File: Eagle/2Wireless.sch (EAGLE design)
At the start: 17 parts, among them IC1 TCA9517A, IC2 VREGLD1117, IC3 MB85RS256TYPNF-G-BCERE1, U1 PHOTON_WITH_HEADERS

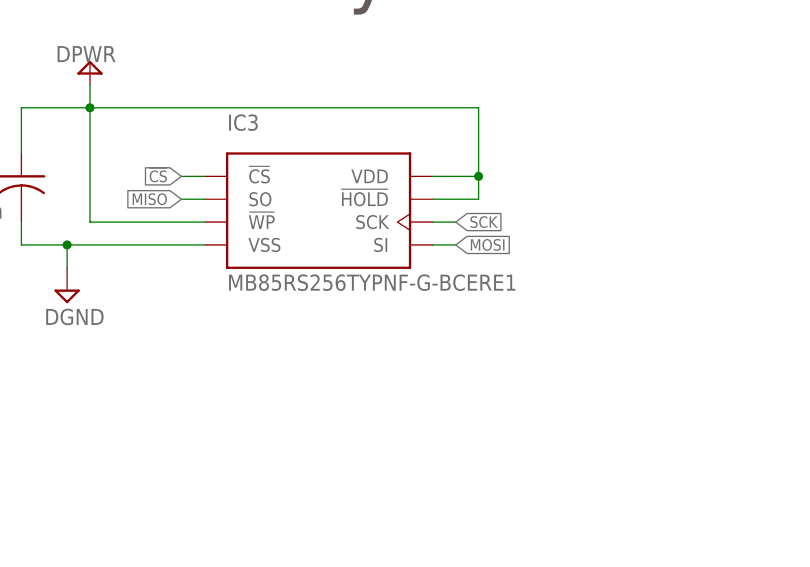
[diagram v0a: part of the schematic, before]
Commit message: Change FRAM to 256k.
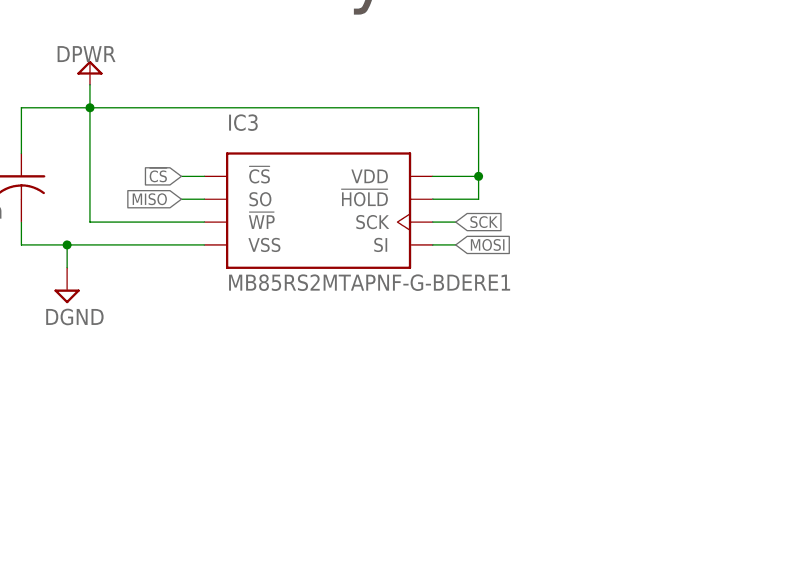
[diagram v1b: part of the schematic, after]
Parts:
- IC3: value MB85RS256TYPNF-G-BCERE1 -> MB85RS2MTAPNF-G-BDERE1
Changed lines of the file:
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@@
 <setting verticaltext="up"/>
 </settings>
-<grid distance="0.1" unitdist="inch" unit="inch" style="lines" multiple="1" display="yes" altdistance="0.01" altunitdist="inch" altunit="inch"/>
+<grid distance="0.1" unitdist="inch" unit="inch" style="lines" multiple="1" display="no" altdistance="0.01" altunitdist="inch" altunit="inch"/>
 <layers>
 <layer number="1" name="Top" color="4" fill="1" visible="no" active="no"/>
@@
 <part name="DGND21" library="studio_h" deviceset="DGND" device=""/>
 <part name="IC2" library="studio_h" deviceset="VREG" device="LD1117"/>
-<part name="IC3" library="studio_h" deviceset="FRAMSPI" device="" value="MB85RS256TYPNF-G-BCERE1"/>
+<part name="IC3" library="studio_h" deviceset="FRAMSPI" device="" value="MB85RS2MTAPNF-G-BDERE1"/>
 <part name="DGND24" library="studio_h" deviceset="DGND" device=""/>
 <part name="C7" library="studio_h" deviceset="C" device="B" value="100n"/>

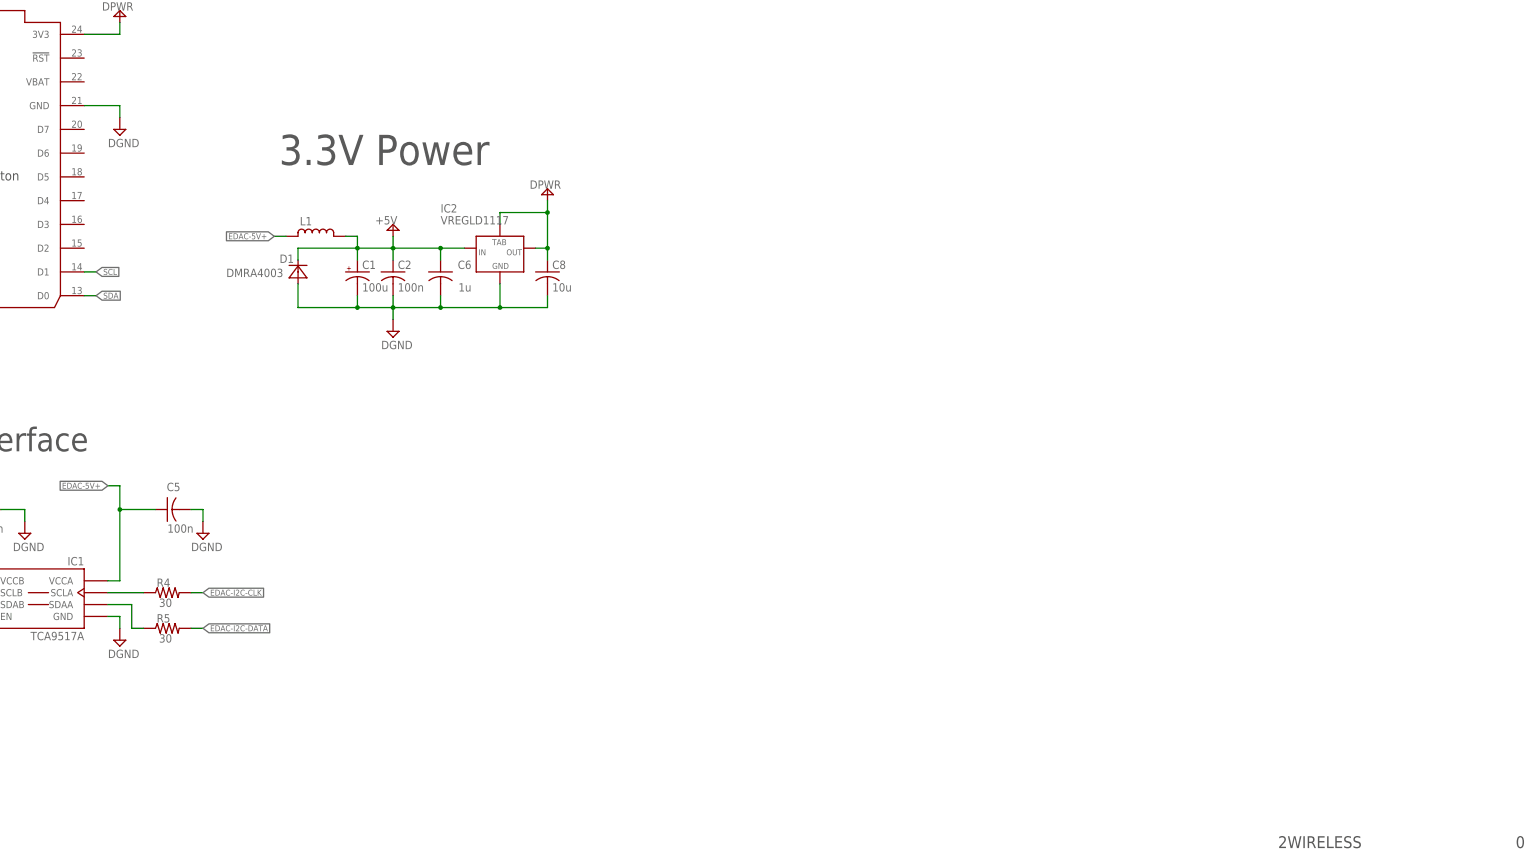
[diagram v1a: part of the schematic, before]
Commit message: Add Primo/V2 version switch.
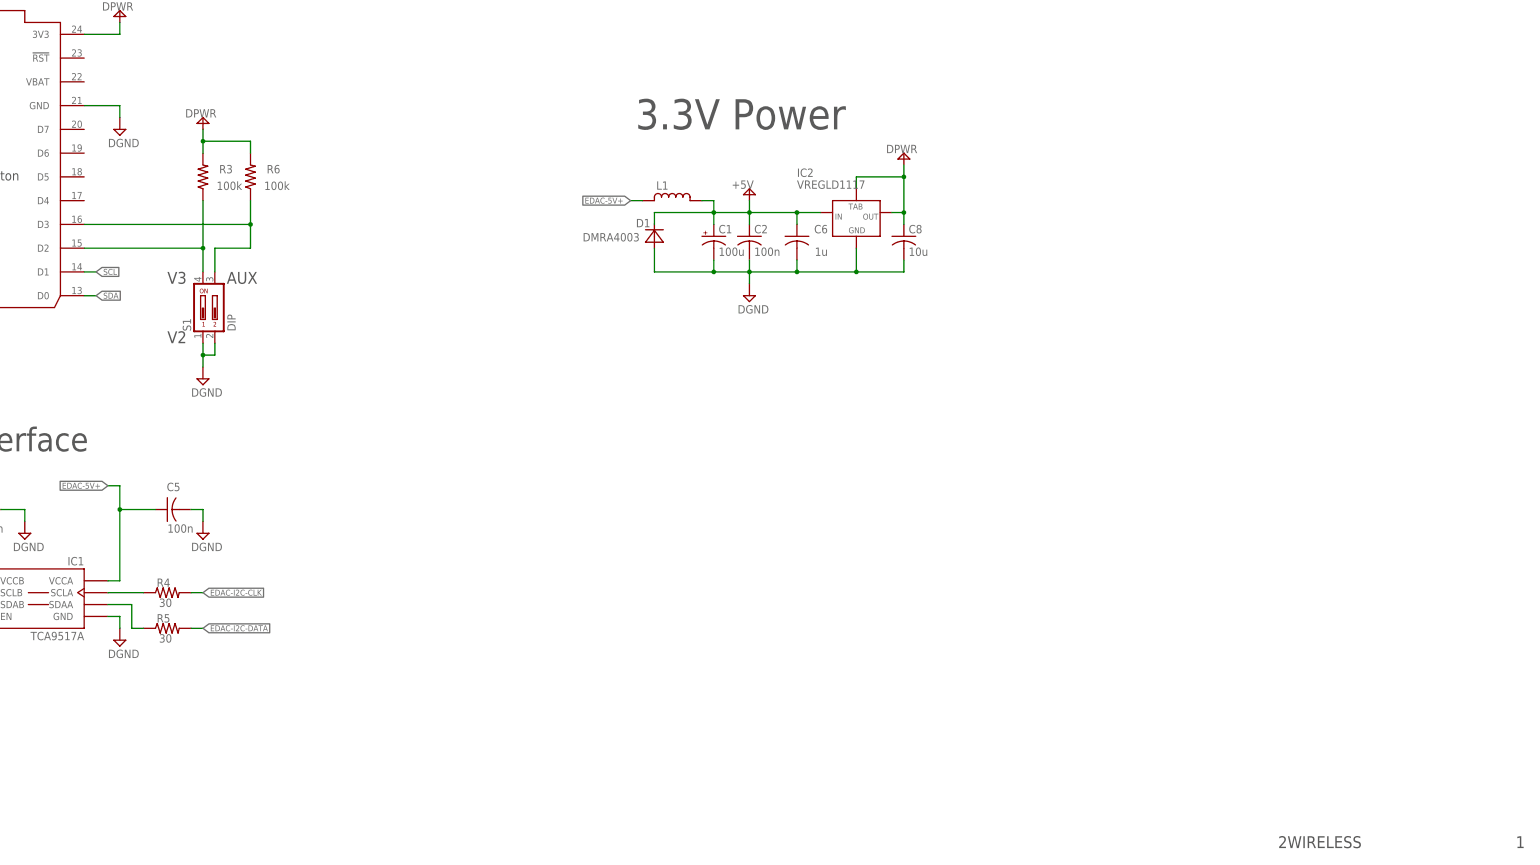
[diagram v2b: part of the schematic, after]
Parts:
- added R3, R6: 100k, studio_h:RB
- added S1: DIP, studio_h:219-02
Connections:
- new net DI-AUX: R6.1, S1.3, U1.D3
- new net DI-VERSION: R3.1, S1.4, U1.D2
- net DGND: now also S1.1, S1.2
- net DPWR: now also R3.2, R6.2
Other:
- note added: "1"
- note added: "AUX"
- note added: "V2"
- note added: "V3"
- note removed: "0"
- moved on the sheet: C1, C2, C6, C8, D1, IC2, L1

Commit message: Add RS232 Connector for future use.
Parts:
- added SV1: (no value), studio_h:MA04-1
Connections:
- new net RX: SV1.4, U1.RX
- new net TX: SV1.3, U1.TX
- net +5V: now also SV1.1
- net DGND: now also SV1.2
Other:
- note added: "2"
- note added: "Male: TE 640456-4 Female: TE 3-640441-4"
- note added: "RS-232"
- note removed: "1"
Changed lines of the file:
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@@
 <part name="DPWR5" library="studio_h" deviceset="DPWR" device=""/>
 <part name="DGND3" library="studio_h" deviceset="DGND" device=""/>
+<part name="SV1" library="studio_h" deviceset="MA04-1" device=""/>
+<part name="DGND4" library="studio_h" deviceset="DGND" device=""/>
 </parts>
 <sheets>
@@
 <plain>
 <text x="367.03" y="6.35" size="2.54" layer="97" font="vector" ratio="12">2WIRELESS</text>
-<text x="417.83" y="6.35" size="2.54" layer="97" font="vector" ratio="12">1</text>
+<text x="417.83" y="6.35" size="2.54" layer="97" font="vector" ratio="12">2</text>
 <text x="229.616" y="160.02" size="6.4516" layer="97" font="vector" ratio="12">3.3V Power</text>
 <text x="237.236" y="233.172" size="6.4516" layer="97" font="vector" ratio="12">Memory</text>
@@
 <text x="129.54" y="114.3" size="2.54" layer="97" font="vector" ratio="12">V2</text>
 <text x="142.24" y="127" size="2.54" layer="97" font="vector" ratio="12">AUX</text>
+<text x="239.776" y="93.98" size="6.4516" layer="97" font="vector" ratio="12">RS-232</text>
+<text x="240.03" y="62.23" size="2.54" layer="97" font="vector" ratio="12">Male: TE 640456-4
+Female: TE 3-640441-4</text>
 </plain>
 <instances>
@@
 </instance>
 <instance part="DGND1" gate="G$1" x="119.38" y="160.02"/>
-<instance part="DGND2" gate="G$1" x="68.58" y="170.18"/>
+<instance part="DGND2" gate="G$1" x="55.88" y="170.18"/>
 <instance part="C4" gate="G$1" x="88.9" y="78.74" smashed="yes" rot="R90">
 <attribute name="NAME" x="91.694" y="84.455" size="1.778" layer="95" font="vector" ratio="12" rot="R180"/>
@@
 <instance part="DPWR5" gate="G$1" x="137.16" y="160.02"/>
 <instance part="DGND3" gate="G$1" x="137.16" y="106.68"/>
+<instance part="SV1" gate="G$1" x="259.08" y="78.74"/>
+<instance part="DGND4" gate="G$1" x="281.94" y="73.66"/>
 </instances>
 <busses>
@@
 <pinref part="U1" gate="G$1" pin="GND@2"/>
 <pinref part="DGND2" gate="G$1" pin="DGND"/>
-<wire x1="76.2" y1="175.26" x2="68.58" y2="175.26" width="0.1524" layer="91"/>
-<wire x1="68.58" y1="175.26" x2="68.58" y2="172.72" width="0.1524" layer="91"/>
+<wire x1="76.2" y1="175.26" x2="55.88" y2="175.26" width="0.1524" layer="91"/>
+<wire x1="55.88" y1="175.26" x2="55.88" y2="172.72" width="0.1524" layer="91"/>
 </segment>
 <segment>
@@
 <wire x1="139.7" y1="111.76" x2="137.16" y2="111.76" width="0.1524" layer="91"/>
 <junction x="137.16" y="111.76"/>
+</segment>
+<segment>
+<pinref part="SV1" gate="G$1" pin="2"/>
+<pinref part="DGND4" gate="G$1" pin="DGND"/>
+<wire x1="264.16" y1="78.74" x2="281.94" y2="78.74" width="0.1524" layer="91"/>
+<wire x1="281.94" y1="78.74" x2="281.94" y2="76.2" width="0.1524" layer="91"/>
 </segment>
 </net>
@@
 <pinref part="IC2" gate="G$1" pin="IN"/>
 </segment>
+<segment>
+<pinref part="SV1" gate="G$1" pin="1"/>
+<wire x1="264.16" y1="76.2" x2="266.7" y2="76.2" width="0.1524" layer="91"/>
+<label x="266.7" y="76.2" size="1.27" layer="95" font="vector" ratio="12" xref="yes"/>
+</segment>
 </net>
 <net name="EDAC-5V+" class="0">
@@
 <segment>
 <pinref part="U1" gate="G$1" pin="A5"/>
-<wire x1="76.2" y1="149.86" x2="71.12" y2="149.86" width="0.1524" layer="91"/>
-<label x="71.12" y="149.86" size="1.27" layer="95" font="vector" ratio="12" rot="R180" xref="yes"/>
+<wire x1="76.2" y1="149.86" x2="73.66" y2="149.86" width="0.1524" layer="91"/>
+<label x="73.66" y="149.86" size="1.27" layer="95" font="vector" ratio="12" rot="R180" xref="yes"/>
 </segment>
 <segment>
@@
 <segment>
 <pinref part="U1" gate="G$1" pin="A4"/>
-<wire x1="76.2" y1="144.78" x2="71.12" y2="144.78" width="0.1524" layer="91"/>
-<label x="71.12" y="144.78" size="1.27" layer="95" font="vector" ratio="12" rot="R180" xref="yes"/>
+<wire x1="76.2" y1="144.78" x2="73.66" y2="144.78" width="0.1524" layer="91"/>
+<label x="73.66" y="144.78" size="1.27" layer="95" font="vector" ratio="12" rot="R180" xref="yes"/>
 </segment>
 <segment>
@@
 <segment>
 <pinref part="U1" gate="G$1" pin="A3"/>
-<wire x1="76.2" y1="139.7" x2="71.12" y2="139.7" width="0.1524" layer="91"/>
-<label x="71.12" y="139.7" size="1.27" layer="95" font="vector" ratio="12" rot="R180" xref="yes"/>
+<wire x1="76.2" y1="139.7" x2="73.66" y2="139.7" width="0.1524" layer="91"/>
+<label x="73.66" y="139.7" size="1.27" layer="95" font="vector" ratio="12" rot="R180" xref="yes"/>
 </segment>
 <segment>
@@
 <segment>
 <pinref part="U1" gate="G$1" pin="A2"/>
-<wire x1="76.2" y1="134.62" x2="71.12" y2="134.62" width="0.1524" layer="91"/>
-<label x="71.12" y="134.62" size="1.27" layer="95" font="vector" ratio="12" rot="R180" xref="yes"/>
+<wire x1="76.2" y1="134.62" x2="73.66" y2="134.62" width="0.1524" layer="91"/>
+<label x="73.66" y="134.62" size="1.27" layer="95" font="vector" ratio="12" rot="R180" xref="yes"/>
 </segment>
 <segment>
@@
 </segment>
 </net>
+<net name="TX" class="0">
+<segment>
+<pinref part="U1" gate="G$1" pin="TX"/>
+<wire x1="76.2" y1="170.18" x2="73.66" y2="170.18" width="0.1524" layer="91"/>
+<label x="73.66" y="170.18" size="1.27" layer="95" font="vector" ratio="12" rot="R180" xref="yes"/>
+</segment>
+<segment>
+<pinref part="SV1" gate="G$1" pin="3"/>
+<wire x1="264.16" y1="81.28" x2="266.7" y2="81.28" width="0.1524" layer="91"/>
+<label x="266.7" y="81.28" size="1.27" layer="95" font="vector" ratio="12" xref="yes"/>
+</segment>
+</net>
+<net name="RX" class="0">
+<segment>
+<pinref part="U1" gate="G$1" pin="RX"/>
+<wire x1="76.2" y1="165.1" x2="73.66" y2="165.1" width="0.1524" layer="91"/>
+<label x="73.66" y="165.1" size="1.27" layer="95" font="vector" ratio="12" rot="R180" xref="yes"/>
+</segment>
+<segment>
+<pinref part="SV1" gate="G$1" pin="4"/>
+<wire x1="264.16" y1="83.82" x2="266.7" y2="83.82" width="0.1524" layer="91"/>
+<label x="266.7" y="83.82" size="1.27" layer="95" font="vector" ratio="12" xref="yes"/>
+</segment>
+</net>

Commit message: Switch layout from Photon to Arduino MKR1000.
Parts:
- removed C8: 10u, studio_h:CG
- removed IC2: VREGLD1117, studio_h:VREGLD1117
- removed R1, R2: 2k, studio_h:RB
- removed SV1: (no value), studio_h:MA04-1
- removed U1: PHOTON_WITH_HEADERS, Particle:PHOTON_WITH_HEADERS
- added J4, J5: (no value), studio_h:MA14-1
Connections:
- removed net RX: SV1.4, U1.RX
- removed net TX: SV1.3, U1.TX
- net !CS: now also J4.13; no longer U1.A2
- net +5V: now also J5.13; no longer IC2.IN, SV1.1
- net DGND: now also J5.11; no longer C8.2, IC2.GND, SV1.2, U1.GND@2, U1.GND@21
- net DI-AUX: now also J4.12; no longer U1.D3
- net DI-VERSION: now also J4.11; no longer U1.D2
- net DPWR: now also J5.12; no longer C8.1, IC2.OUT, IC2.TAB, R1.2, R2.2, U1.3V3
- net MISO: now also J5.5; no longer U1.A4
- net MOSI: now also J5.3; no longer U1.A5
- net SCK: now also J5.4; no longer U1.A3
- net SCL: now also J5.7; no longer R1.1, U1.D1
- net SDA: now also J5.6; no longer R2.1, U1.D0
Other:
- note added: "3"
- note added: "5V Power"
- note added: "Arduino MKR1000"
- note removed: "2"
- note removed: "3.3V Power"
- note removed: "Male: TE 640456-4 Female: TE 3-640441-4"
- note removed: "Particle Photon"
- note removed: "RS-232"
- note removed: "https://docs.particle.io/datasheets/wi-fi/photon-datasheet/"
- moved on the sheet: R3, R6, S1

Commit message: Add I2C pullups to MKR1000 layout.
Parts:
- added R1, R2: 2k, studio_h:RB
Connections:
- net DPWR: now also R1.2, R2.2
- net SCL: now also R1.1
- net SDA: now also R2.1
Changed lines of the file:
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@@
 <part name="DPWR4" library="studio_h" deviceset="DPWR" device=""/>
 <part name="DGND1" library="studio_h" deviceset="DGND" device=""/>
+<part name="R1" library="studio_h" deviceset="R" device="B" value="2k"/>
+<part name="R2" library="studio_h" deviceset="R" device="B" value="2k"/>
 </parts>
 <sheets>
@@
 <instance part="DPWR4" gate="G$1" x="129.54" y="185.42"/>
 <instance part="DGND1" gate="G$1" x="129.54" y="175.26"/>
+<instance part="R1" gate="G$1" x="63.5" y="71.12" smashed="yes" rot="R90">
+<attribute name="NAME" x="69.8754" y="73.66" size="1.778" layer="95" font="vector" ratio="12" rot="R180"/>
+<attribute name="VALUE" x="69.342" y="70.104" size="1.778" layer="96" font="vector" ratio="12" rot="R180"/>
+</instance>
+<instance part="R2" gate="G$1" x="73.66" y="71.12" smashed="yes" rot="R90">
+<attribute name="NAME" x="80.0354" y="73.66" size="1.778" layer="95" font="vector" ratio="12" rot="R180"/>
+<attribute name="VALUE" x="79.502" y="70.104" size="1.778" layer="96" font="vector" ratio="12" rot="R180"/>
+</instance>
 </instances>
 <busses>
@@
 <label x="58.42" y="60.96" size="1.27" layer="95" font="vector" ratio="12" rot="R180" xref="yes"/>
 <pinref part="IC1" gate="G$1" pin="SCLB"/>
-<wire x1="86.36" y1="60.96" x2="58.42" y2="60.96" width="0.1524" layer="91"/>
+<wire x1="86.36" y1="60.96" x2="63.5" y2="60.96" width="0.1524" layer="91"/>
+<pinref part="R1" gate="G$1" pin="1"/>
+<wire x1="63.5" y1="60.96" x2="58.42" y2="60.96" width="0.1524" layer="91"/>
+<wire x1="63.5" y1="66.04" x2="63.5" y2="60.96" width="0.1524" layer="91"/>
+<junction x="63.5" y="60.96"/>
 </segment>
 <segment>
@@
 <segment>
 <label x="58.42" y="58.42" size="1.27" layer="95" font="vector" ratio="12" rot="R180" xref="yes"/>
-<wire x1="86.36" y1="58.42" x2="58.42" y2="58.42" width="0.1524" layer="91"/>
+<wire x1="86.36" y1="58.42" x2="73.66" y2="58.42" width="0.1524" layer="91"/>
 <pinref part="IC1" gate="G$1" pin="SDAB"/>
+<pinref part="R2" gate="G$1" pin="1"/>
+<wire x1="73.66" y1="58.42" x2="58.42" y2="58.42" width="0.1524" layer="91"/>
+<wire x1="73.66" y1="66.04" x2="73.66" y2="58.42" width="0.1524" layer="91"/>
+<junction x="73.66" y="58.42"/>
 </segment>
 <segment>
@@
 <wire x1="86.36" y1="63.5" x2="83.82" y2="63.5" width="0.1524" layer="91"/>
 <pinref part="DPWR1" gate="G$1" pin="DPWR"/>
-</segment>
-<segment>
+<pinref part="R2" gate="G$1" pin="2"/>
+<wire x1="73.66" y1="76.2" x2="73.66" y2="78.74" width="0.1524" layer="91"/>
+<pinref part="R1" gate="G$1" pin="2"/>
+<wire x1="63.5" y1="76.2" x2="63.5" y2="78.74" width="0.1524" layer="91"/>
+<wire x1="63.5" y1="78.74" x2="73.66" y2="78.74" width="0.1524" layer="91"/>
+<wire x1="73.66" y1="78.74" x2="83.82" y2="78.74" width="0.1524" layer="91"/>
+<junction x="73.66" y="78.74"/>
+</segment>
+<segment>

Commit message: Change power source on TCA9517A.
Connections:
- net +5V: now also C5.1, IC1.VCCA
- net EDAC-5V+: no longer C5.1, IC1.VCCA
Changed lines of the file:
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@@
 <setting verticaltext="up"/>
 </settings>
-<grid distance="0.1" unitdist="inch" unit="inch" style="lines" multiple="1" display="yes" altdistance="0.01" altunitdist="inch" altunit="inch"/>
+<grid distance="0.1" unitdist="inch" unit="inch" style="lines" multiple="1" display="no" altdistance="0.01" altunitdist="inch" altunit="inch"/>
 <layers>
 <layer number="1" name="Top" color="4" fill="1" visible="no" active="no"/>
@@
 <pinref part="J5" gate="G$1" pin="13"/>
 </segment>
-</net>
-<net name="EDAC-5V+" class="0">
-<segment>
-<pinref part="L1" gate="G$1" pin="1"/>
-<wire x1="231.14" y1="144.78" x2="228.6" y2="144.78" width="0.1524" layer="91"/>
-<label x="228.6" y="144.78" size="1.27" layer="95" font="vector" ratio="12" rot="R180" xref="yes"/>
-</segment>
 <segment>
 <pinref part="IC1" gate="G$1" pin="VCCA"/>
@@
 <pinref part="C5" gate="G$1" pin="1"/>
 <wire x1="119.38" y1="78.74" x2="127" y2="78.74" width="0.1524" layer="91"/>
+<wire x1="119.38" y1="78.74" x2="119.38" y2="81.28" width="0.1524" layer="91"/>
 <junction x="119.38" y="78.74"/>
-<wire x1="119.38" y1="78.74" x2="119.38" y2="83.82" width="0.1524" layer="91"/>
-<wire x1="119.38" y1="83.82" x2="116.84" y2="83.82" width="0.1524" layer="91"/>
-<label x="116.84" y="83.82" size="1.27" layer="95" font="vector" ratio="12" rot="R180" xref="yes"/>
+<label x="119.38" y="81.28" size="1.27" layer="95" font="vector" ratio="12" rot="R90" xref="yes"/>
 </segment>
 </net>
+<net name="EDAC-5V+" class="0">
+<segment>
+<pinref part="L1" gate="G$1" pin="1"/>
+<wire x1="231.14" y1="144.78" x2="228.6" y2="144.78" width="0.1524" layer="91"/>
+<label x="228.6" y="144.78" size="1.27" layer="95" font="vector" ratio="12" rot="R180" xref="yes"/>
+</segment>
+</net>
